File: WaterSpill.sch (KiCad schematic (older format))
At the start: 29 parts, among them J1 Conn_01x03_Male, J2 Conn_01x02_Male, J3 Conn_01x03_Male, J4 Conn_01x03_Male, J5 Conn_01x02_Male, Q1 2N3904, SW1 SW_Push, SW2 SW_Push, U1 ESP-12E, U2 74HC132

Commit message: Silk Screen text added
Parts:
- Q1: symbol dk_Transistors-Bipolar-BJT-Single:2N3904 -> WaterSpill-rescue:2N3904-dk_Transistors-Bipolar-BJT-Single
- U1: symbol ESP8266:ESP-12E -> WaterSpill-rescue:ESP-12E-ESP8266
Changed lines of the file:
@@
 Sheet 1 1
 Title "ESP8266 Water Spill Module"
-Date ""
-Rev "1.1"
+Date "2019-01-23"
+Rev "1.2"
 Comp ""
 Comment1 "Rev 1.1: Added CH_PD 6800pF Capacitor"
-Comment2 ""
+Comment2 "Rev 1.2: Added Active input at J2 through 2N3904 Transistor"
 Comment3 ""
 Comment4 ""
@@
 $EndComp
 $Comp
-L ESP8266:ESP-12E U1
+L WaterSpill-rescue:ESP-12E-ESP8266 U1
 U 1 1 5A7F1FAC
 P 5800 2250
@@
 	1    0    0    -1
 $EndComp
-Text Label 650  5300 0    60   ~ 0
+Text Label 850  5350 0    60   ~ 0
 WaterOrSmoke
 $Comp
@@
 	-1   0    0    1
 $EndComp
-Text Label 9000 3450 0    60   ~ 0
-NotUsed
+Text Label 9100 3450 0    60   ~ 0
+A2D
 Wire Wire Line
 	3800 1050 3800 1100
@@
 	2250 5100 2600 5100
 $Comp
-L dk_Transistors-Bipolar-BJT-Single:2N3904 Q1
+L WaterSpill-rescue:2N3904-dk_Transistors-Bipolar-BJT-Single Q1
 U 1 1 5C47388D
 P 1250 6600

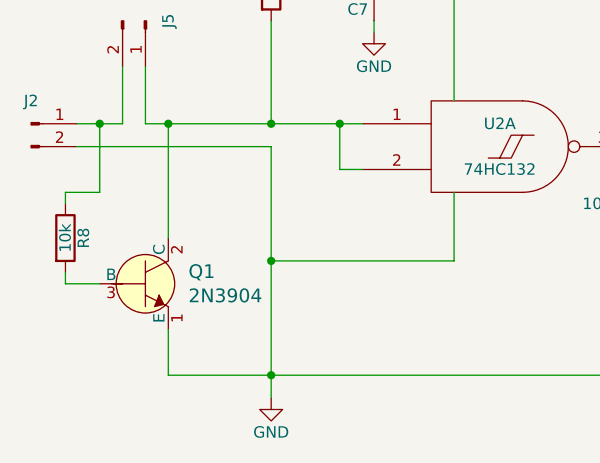
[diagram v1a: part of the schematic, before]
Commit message: Corrected transistor footprint
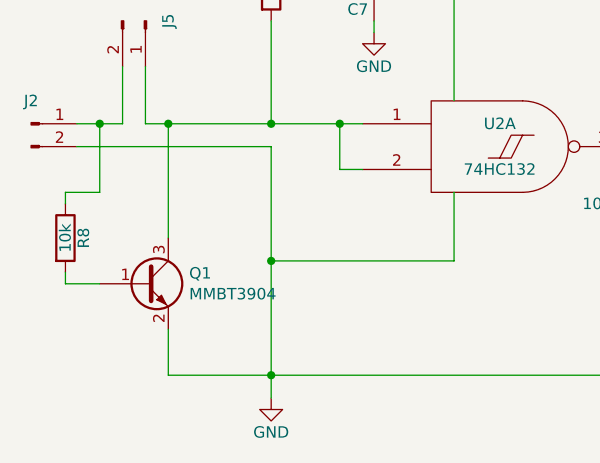
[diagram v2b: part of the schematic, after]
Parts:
- removed Q1: 2N3904, digikey-footprints:TO-92-3, symbol WaterSpill-rescue:2N3904-dk_Transistors-Bipolar-BJT-Single
- added Q1: MMBT3904, Package_TO_SOT_SMD:SOT-23, symbol Transistor_BJT:MMBT3904
- BT1, J2, J5: footprint (none) -> Pin_Headers:Pin_Header_Straight_1x02_Pitch2.54mm
- C1, C2, C3, C4, C5, C7: footprint (none) -> Capacitors_SMD:C_0805_HandSoldering
- D1: footprint (none) -> Diodes_SMD:D_SOD-323_HandSoldering
- J1, J3, J4: footprint (none) -> Pin_Headers:Pin_Header_Straight_1x03_Pitch2.54mm
- R1, R10, R11, R2, R3, R4, R5, R6, R7, R8, R9: footprint (none) -> Resistors_SMD:R_0805_HandSoldering
- SW1, SW2: footprint (none) -> Buttons_Switches_SMD:SW_SPST_FSMSM
- U1: footprint (none) -> ESP8266:ESP-12E_SMD
- U2: footprint (none) -> Housings_SOIC:SOIC-14_3.9x8.7mm_Pitch1.27mm
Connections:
- net GND: now also Q1.2 (E)
- net at J5.1 (Pin_1), R7.2, U2.1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: now also Q1.3 (C)
- net at R8.2: now also Q1.1 (B)
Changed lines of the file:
@@
 F 0 "U1" H 5800 2150 50  0000 C CNN
 F 1 "ESP-12E" H 5800 2350 50  0000 C CNN
-F 2 "" H 5800 2250 50  0001 C CNN
+F 2 "ESP8266:ESP-12E_SMD" H 5800 2250 50  0001 C CNN
 F 3 "" H 5800 2250 50  0001 C CNN
 	1    5800 2250
@@
 F 0 "R1" V 4180 1300 50  0000 C CNN
 F 1 "10k" V 4100 1300 50  0000 C CNN
-F 2 "" V 4030 1300 50  0001 C CNN
+F 2 "Resistors_SMD:R_0805_HandSoldering" V 4030 1300 50  0001 C CNN
 F 3 "" H 4100 1300 50  0001 C CNN
 	1    4100 1300
@@
 F 0 "R2" V 4380 1300 50  0000 C CNN
 F 1 "10k" V 4300 1300 50  0000 C CNN
-F 2 "" V 4230 1300 50  0001 C CNN
+F 2 "Resistors_SMD:R_0805_HandSoldering" V 4230 1300 50  0001 C CNN
 F 3 "" H 4300 1300 50  0001 C CNN
 	1    4300 1300
@@
 F 0 "R6" V 6930 3000 50  0000 C CNN
 F 1 "10k" V 6850 3000 50  0000 C CNN
-F 2 "" V 6780 3000 50  0001 C CNN
+F 2 "Resistors_SMD:R_0805_HandSoldering" V 6780 3000 50  0001 C CNN
 F 3 "" H 6850 3000 50  0001 C CNN
 	1    6850 3000
@@
 F 0 "R4" V 6930 1300 50  0000 C CNN
 F 1 "10k" V 6850 1300 50  0000 C CNN
-F 2 "" V 6780 1300 50  0001 C CNN
+F 2 "Resistors_SMD:R_0805_HandSoldering" V 6780 1300 50  0001 C CNN
 F 3 "" H 6850 1300 50  0001 C CNN
 	1    6850 1300
@@
 F 0 "R5" V 7180 1300 50  0000 C CNN
 F 1 "10k" V 7100 1300 50  0000 C CNN
-F 2 "" V 7030 1300 50  0001 C CNN
+F 2 "Resistors_SMD:R_0805_HandSoldering" V 7030 1300 50  0001 C CNN
 F 3 "" H 7100 1300 50  0001 C CNN
 	1    7100 1300
@@
 F 0 "SW1" H 6900 3950 50  0000 L CNN
 F 1 "SW_Push" H 6850 3790 50  0001 C CNN
-F 2 "" H 6850 4050 50  0001 C CNN
+F 2 "Buttons_Switches_SMD:SW_SPST_FSMSM" H 6850 4050 50  0001 C CNN
 F 3 "" H 6850 4050 50  0001 C CNN
 	1    6850 3850
@@
 F 0 "SW2" H 6900 4300 50  0000 L CNN
 F 1 "SW_Push" H 6850 4140 50  0001 C CNN
-F 2 "" H 6850 4400 50  0001 C CNN
+F 2 "Buttons_Switches_SMD:SW_SPST_FSMSM" H 6850 4400 50  0001 C CNN
 F 3 "" H 6850 4400 50  0001 C CNN
 	1    6850 4200
@@
 F 0 "J1" V 8150 5200 50  0000 C CNN
 F 1 "Conn_01x03_Male" V 8150 4800 50  0001 C TNN
-F 2 "" H 8150 5000 50  0001 C CNN
+F 2 "Pin_Headers:Pin_Header_Straight_1x03_Pitch2.54mm" H 8150 5000 50  0001 C CNN
 F 3 "" H 8150 5000 50  0001 C CNN
 	1    8150 5000
@@
 F 0 "D1" H 8400 4350 50  0000 C CNN
 F 1 "1N4148" H 8400 4150 50  0000 C CNN
-F 2 "" H 8400 4250 50  0001 C CNN
+F 2 "Diodes_SMD:D_SOD-323_HandSoldering" H 8400 4250 50  0001 C CNN
 F 3 "" H 8400 4250 50  0001 C CNN
 	1    8400 4250
@@
 F 0 "U2" H 2800 6100 50  0000 C CNN
 F 1 "74HC132" H 2800 5900 50  0000 C CNN
-F 2 "" H 2800 6000 50  0001 C CNN
+F 2 "Housings_SOIC:SOIC-14_3.9x8.7mm_Pitch1.27mm" H 2800 6000 50  0001 C CNN
 F 3 "" H 2800 6000 50  0001 C CNN
 	1    2800 6000
@@
 F 0 "J2" H 750 6000 50  0000 C CNN
 F 1 "Conn_01x02_Male" V 750 5700 50  0001 C CNN
-F 2 "" H 750 5900 50  0001 C CNN
+F 2 "Pin_Headers:Pin_Header_Straight_1x02_Pitch2.54mm" H 750 5900 50  0001 C CNN
 F 3 "" H 750 5900 50  0001 C CNN
 	1    750  5900
@@
 F 0 "R7" V 1880 5300 50  0000 C CNN
 F 1 "1M" V 1800 5300 50  0000 C CNN
-F 2 "" V 1730 5300 50  0001 C CNN
+F 2 "Resistors_SMD:R_0805_HandSoldering" V 1730 5300 50  0001 C CNN
 F 3 "" H 1800 5300 50  0001 C CNN
 	1    1800 5300
@@
 F 0 "U2" H 4350 6200 50  0000 C CNN
 F 1 "74HC132" H 4350 6000 50  0000 C CNN
-F 2 "" H 4350 6100 50  0001 C CNN
+F 2 "Housings_SOIC:SOIC-14_3.9x8.7mm_Pitch1.27mm" H 4350 6100 50  0001 C CNN
 F 3 "" H 4350 6100 50  0001 C CNN
 	2    4350 6100
@@
 F 0 "C2" H 3425 6450 50  0000 L CNN
 F 1 "100nF" H 3425 6250 50  0000 L CNN
-F 2 "" H 3438 6200 50  0001 C CNN
+F 2 "Capacitors_SMD:C_0805_HandSoldering" H 3438 6200 50  0001 C CNN
 F 3 "" H 3400 6350 50  0001 C CNN
 	1    3400 6350
@@
 F 0 "R9" V 3730 6750 50  0000 C CNN
 F 1 "4M7" V 3650 6750 50  0000 C CNN
-F 2 "" V 3580 6750 50  0001 C CNN
+F 2 "Resistors_SMD:R_0805_HandSoldering" V 3580 6750 50  0001 C CNN
 F 3 "" H 3650 6750 50  0001 C CNN
 	1    3650 6750
@@
 F 0 "U2" H 5800 6100 50  0000 C CNN
 F 1 "74HC132" H 5800 5900 50  0000 C CNN
-F 2 "" H 5800 6000 50  0001 C CNN
+F 2 "Housings_SOIC:SOIC-14_3.9x8.7mm_Pitch1.27mm" H 5800 6000 50  0001 C CNN
 F 3 "" H 5800 6000 50  0001 C CNN
 	4    5800 6000
@@
 F 0 "U2" H 7200 6200 50  0000 C CNN
 F 1 "74HC132" H 7200 6000 50  0000 C CNN
-F 2 "" H 7200 6100 50  0001 C CNN
+F 2 "Housings_SOIC:SOIC-14_3.9x8.7mm_Pitch1.27mm" H 7200 6100 50  0001 C CNN
 F 3 "" H 7200 6100 50  0001 C CNN
 	3    7200 6100
@@
 F 0 "C1" H 4675 3000 50  0000 L CNN
 F 1 "6800pF" H 4675 2800 50  0000 L CNN
-F 2 "" H 4688 2750 50  0001 C CNN
+F 2 "Capacitors_SMD:C_0805_HandSoldering" H 4688 2750 50  0001 C CNN
 F 3 "" H 4650 2900 50  0001 C CNN
 	1    4650 2900
@@
 F 0 "R3" V 4580 1300 50  0000 C CNN
 F 1 "10k" V 4500 1300 50  0000 C CNN
-F 2 "" V 4430 1300 50  0001 C CNN
+F 2 "Resistors_SMD:R_0805_HandSoldering" V 4430 1300 50  0001 C CNN
 F 3 "" H 4500 1300 50  0001 C CNN
 	1    4500 1300
@@
 F 0 "BT1" H 1650 3450 50  0001 C BNN
 F 1 "Battery" H 1650 3350 50  0001 L CNN
-F 2 "" V 1550 3410 50  0001 C CNN
+F 2 "Pin_Headers:Pin_Header_Straight_1x02_Pitch2.54mm" V 1550 3410 50  0001 C CNN
 F 3 "" V 1550 3410 50  0001 C CNN
 	1    1550 3350
@@
 F 0 "C3" H 1925 3450 50  0000 L CNN
 F 1 "10uF" H 1925 3250 50  0000 L CNN
-F 2 "" H 1938 3200 50  0001 C CNN
+F 2 "Capacitors_SMD:C_0805_HandSoldering" H 1938 3200 50  0001 C CNN
 F 3 "" H 1900 3350 50  0001 C CNN
 	1    1900 3350
@@
 F 0 "C4" H 2175 3450 50  0000 L CNN
 F 1 "10uF" H 2175 3250 50  0000 L CNN
-F 2 "" H 2188 3200 50  0001 C CNN
+F 2 "Capacitors_SMD:C_0805_HandSoldering" H 2188 3200 50  0001 C CNN
 F 3 "" H 2150 3350 50  0001 C CNN
 	1    2150 3350
@@
 F 0 "R11" V 9230 2850 50  0000 C CNN
 F 1 "130K" V 9150 2850 50  0000 C CNN
-F 2 "" V 9080 2850 50  0001 C CNN
+F 2 "Resistors_SMD:R_0805_HandSoldering" V 9080 2850 50  0001 C CNN
 F 3 "" H 9150 2850 50  0001 C CNN
 	1    9150 2850
@@
 F 0 "C5" H 8925 2950 50  0000 L CNN
 F 1 "10nF" H 8925 2750 50  0000 R CNN
-F 2 "" H 8938 2700 50  0001 C CNN
+F 2 "Capacitors_SMD:C_0805_HandSoldering" H 8938 2700 50  0001 C CNN
 F 3 "" H 8900 2850 50  0001 C CNN
 	1    8900 2850
@@
 F 0 "R10" V 9230 2350 50  0000 C CNN
 F 1 "330K" V 9150 2350 50  0000 C CNN
-F 2 "" V 9080 2350 50  0001 C CNN
+F 2 "Resistors_SMD:R_0805_HandSoldering" V 9080 2350 50  0001 C CNN
 F 3 "" H 9150 2350 50  0001 C CNN
 	1    9150 2350
@@
 F 0 "J3" V 9900 2800 50  0000 C CNN
 F 1 "Conn_01x03_Male" V 9900 2400 50  0001 C TNN
-F 2 "" H 9900 2600 50  0001 C CNN
+F 2 "Pin_Headers:Pin_Header_Straight_1x03_Pitch2.54mm" H 9900 2600 50  0001 C CNN
 F 3 "" H 9900 2600 50  0001 C CNN
 	1    9900 2600
@@
 F 0 "C7" H 2275 5400 50  0000 L CNN
 F 1 "100nF" H 2275 5200 50  0000 L CNN
-F 2 "" H 2288 5150 50  0001 C CNN
+F 2 "Capacitors_SMD:C_0805_HandSoldering" H 2288 5150 50  0001 C CNN
 F 3 "" H 2250 5300 50  0001 C CNN
 	1    2250 5300
@@
 	2250 5100 2600 5100
 $Comp
-L WaterSpill-rescue:2N3904-dk_Transistors-Bipolar-BJT-Single Q1
-U 1 1 5C47388D
-P 1250 6600
-F 0 "Q1" H 1438 6653 60  0000 L CNN
-F 1 "2N3904" H 1438 6547 60  0000 L CNN
-F 2 "digikey-footprints:TO-92-3" H 1450 6800 60  0001 L CNN
-F 3 "https://my.centralsemi.com/get_document.php?cmp=1&mergetype=pd&mergepath=pd&pdf_id=LSSGP072.PDF" H 1450 6900 60  0001 L CNN
-F 4 "2N3904CS-ND" H 1450 7000 60  0001 L CNN "Digi-Key_PN"
-F 5 "2N3904" H 1450 7100 60  0001 L CNN "MPN"
-F 6 "Discrete Semiconductor Products" H 1450 7200 60  0001 L CNN "Category"
-F 7 "Transistors - Bipolar (BJT) - Single" H 1450 7300 60  0001 L CNN "Family"
-F 8 "https://my.centralsemi.com/get_document.php?cmp=1&mergetype=pd&mergepath=pd&pdf_id=LSSGP072.PDF" H 1450 7400 60  0001 L CNN "DK_Datasheet_Link"
-F 9 "/product-detail/en/central-semiconductor-corp/2N3904/2N3904CS-ND/4806876" H 1450 7500 60  0001 L CNN "DK_Detail_Page"
-F 10 "TRANS NPN 40V TO-92" H 1450 7600 60  0001 L CNN "Description"
-F 11 "Central Semiconductor Corp" H 1450 7700 60  0001 L CNN "Manufacturer"
-F 12 "Active" H 1450 7800 60  0001 L CNN "Status"
-	1    1250 6600
-	1    0    0    -1
-$EndComp
-$Comp
 L WaterSpill-rescue:R-device R8
 U 1 1 5C4E5B99
@@
 F 0 "R8" V 980 6400 50  0000 C CNN
 F 1 "10k" V 900 6400 50  0000 C CNN
-F 2 "" V 830 6400 50  0001 C CNN
+F 2 "Resistors_SMD:R_0805_HandSoldering" V 830 6400 50  0001 C CNN
 F 3 "" H 900 6400 50  0001 C CNN
 	1    900  6400
@@
 F 0 "J4" V 4300 5000 50  0000 C CNN
 F 1 "Conn_01x03_Male" V 4300 4600 50  0001 C TNN
-F 2 "" H 4300 4800 50  0001 C CNN
+F 2 "Pin_Headers:Pin_Header_Straight_1x03_Pitch2.54mm" H 4300 4800 50  0001 C CNN
 F 3 "" H 4300 4800 50  0001 C CNN
 	1    4300 4800
@@
 F 0 "J5" H 1250 5550 50  0000 C CNN
 F 1 "Conn_01x02_Male" V 1250 5250 50  0001 C CNN
-F 2 "" H 1250 5450 50  0001 C CNN
+F 2 "Pin_Headers:Pin_Header_Straight_1x02_Pitch2.54mm" H 1250 5450 50  0001 C CNN
 F 3 "" H 1250 5450 50  0001 C CNN
 	1    1250 5450
@@
 	3400 4350 3400 6000
 Connection ~ 3400 6000
+$Comp
+L Transistor_BJT:MMBT3904 Q1
+U 1 1 5C4A520B
+P 1250 6600
+F 0 "Q1" H 1441 6646 50  0000 L CNN
+F 1 "MMBT3904" H 1441 6555 50  0000 L CNN
+F 2 "Package_TO_SOT_SMD:SOT-23" H 1450 6525 50  0001 L CIN
+F 3 "https://www.fairchildsemi.com/datasheets/2N/2N3904.pdf" H 1250 6600 50  0001 L CNN
+	1    1250 6600
+	1    0    0    -1
+$EndComp
 $EndSCHEMATC
